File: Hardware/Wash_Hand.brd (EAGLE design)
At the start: 71.1 x 48.3 mm, 87 parts, among them IC1 LM358D, IC2 LP298XS, IC3 405016TSSOP, J1 I2C, J2 ICSP, J3 SPI, J4 9V_CONN, J5 EXT_VCC, J6 6_PIN_SERIAL_CABLEPTH, Q1 16.0 Mhz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

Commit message: RELEASE-1.4-rc2
Signed-off-by: Konrad Rzeszutek Wilk <konrad@kernel.org>
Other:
- board text added: "v1.4-rc2"
- board text removed: "v1.4-rc1"
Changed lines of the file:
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@@
 <circle x="8.636" y="38.862" radius="0.254" width="0.254" layer="25"/>
 <circle x="8.636" y="38.862" radius="0.567959375" width="0.1524" layer="25"/>
-<text x="33.02" y="5.842" size="1.778" layer="26" ratio="14" rot="MR0">v1.4-rc1</text>
+<text x="33.02" y="5.842" size="1.778" layer="26" ratio="14" rot="MR0">v1.4-rc2</text>
 <text x="54.356" y="18.796" size="1.016" layer="25" ratio="14">#
 [  ]

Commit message: Board/Schematic: Add PNP to turn on/off the line sensor
.. which we don't have to have on all the time.

Signed-off-by: Konrad Rzeszutek Wilk <konrad@kernel.org>
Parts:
- added T1: PNP, zetex:SOT-23
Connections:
- new net ON_OFF_PNP: T1.3, U2.22
- net VCC: now also T1.2
- net V_POS: now also T1.1
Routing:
- net ON_OFF_PNP: track 0.00 -> 59.3 mm, vias 0 -> 4
- net V_POS: track 33.5 -> 37.3 mm
- net VCC: track 247.9 -> 249.3 mm
- net D0: track 108.8 -> 107.6 mm
- net TX: track 59.1 -> 58.0 mm
- net D: track 12.8 -> 13.4 mm

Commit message: Board/Schematic: Remove 1K by RST/DTR
We haven't used it for two releases and it does
not help with DTR at all.

Signed-off-by: Konrad Rzeszutek Wilk <konrad@kernel.org>
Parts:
- removed R12: 1K, darnok_common:1206
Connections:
- net 0: no longer R12.1
- net RESET: no longer R12.2
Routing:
- net 0: track 390.9 -> 385.3 mm
- net RESET: track 59.3 -> 57.5 mm
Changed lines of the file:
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@@
 <attribute name="VALUE" x="35.56" y="19.304" size="0.6096" layer="27" font="vector" ratio="20" rot="R180" align="bottom-center"/>
-</element>
-<element name="R12" library="darnok_common" package="1206" value="1K" x="23.876" y="10.414" smashed="yes" rot="R90">
-<attribute name="NAME" x="25.527" y="11.43" size="0.6096" layer="25" font="vector" ratio="20" rot="R90" align="bottom-center"/>
-<attribute name="VALUE" x="25.273" y="8.636" size="0.6096" layer="27" font="vector" ratio="20" rot="R90" align="top-center"/>
 </element>
 <element name="R13" library="darnok_common" package="1206" value="1M" x="46.736" y="15.494" smashed="yes" rot="R270">
@@
 <contactref element="U2" pad="29"/>
 <contactref element="J2" pad="5"/>
-<contactref element="R12" pad="2"/>
 <wire x1="60.706" y1="2.286" x2="60.706" y2="8.636" width="0.3048" layer="16"/>
 <wire x1="55.626" y1="2.54" x2="57.404" y2="0.762" width="0.3048" layer="16" curve="90"/>
@@
 <wire x1="25.784" y1="11.814" x2="25.654" y2="11.684" width="0.3048" layer="1" curve="90"/>
 <via x="25.654" y="11.684" extent="1-16" drill="0.35"/>
-<wire x1="25.654" y1="11.684" x2="24.006" y2="11.684" width="0.3048" layer="1"/>
-<wire x1="24.006" y1="11.684" x2="23.876" y2="11.814" width="0.3048" layer="1" curve="-90"/>
 <wire x1="25.654" y1="11.684" x2="25.784" y2="11.814" width="0.3048" layer="1" curve="-90"/>
 <wire x1="25.784" y1="11.814" x2="27.432" y2="11.814" width="0.3048" layer="1"/>
@@
 <contactref element="C2" pad="2"/>
 <contactref element="C1" pad="2"/>
-<contactref element="R12" pad="1"/>
 <contactref element="Y1" pad="2"/>
 <wire x1="27.432" y1="15.618" x2="29.24405" y2="13.29795" width="0.3048" layer="1"/>
@@
 <wire x1="7.366" y1="10.414" x2="7.366" y2="9.398" width="0.3048" layer="1"/>
 <wire x1="7.366" y1="9.398" x2="8.128" y2="8.636" width="0.3048" layer="1"/>
-<wire x1="23.876" y1="9.014" x2="18.288" y2="9.014" width="0.3048" layer="1"/>
 <wire x1="11.176" y1="9.014" x2="7.75" y2="9.014" width="0.3048" layer="1"/>
 <wire x1="7.75" y1="9.014" x2="7.366" y2="9.398" width="0.3048" layer="1" curve="-90"/>

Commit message: Board/Schematic: Rotate LED2 around..
We been soldering it the right way but the schematic
has it turned around.

Signed-off-by: Konrad Rzeszutek Wilk <konrad@kernel.org>
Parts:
- turned LED2 to 90 degrees
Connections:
- removed net INT_LED: LED2.C, R17.2
- new net N$15: LED2.A, R17.2
- net 0: now also LED2.C; no longer LED2.A
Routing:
- net N$15: track 0.00 -> 3.78 mm
- net INT_LED: track 3.78 -> 0.00 mm
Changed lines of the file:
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@@
 <attribute name="VALUE" x="62.865" y="16.256" size="0.6096" layer="27" font="vector" ratio="20" rot="R90" align="top-center"/>
 </element>
-<element name="LED2" library="adafruit" library_urn="urn:adsk.eagle:library:420" package="1206" package3d_urn="urn:adsk.eagle:package:6240349/1" value="" x="61.468" y="21.59" smashed="yes" rot="R270">
-<attribute name="NAME" x="62.738" y="22.86" size="0.6096" layer="25" rot="R270"/>
-<attribute name="VALUE" x="58.928" y="22.86" size="1.27" layer="27" rot="R270"/>
+<element name="LED2" library="adafruit" library_urn="urn:adsk.eagle:library:420" package="1206" package3d_urn="urn:adsk.eagle:package:6240349/1" value="" x="61.468" y="21.59" smashed="yes" rot="R90">
+<attribute name="NAME" x="60.198" y="20.32" size="0.6096" layer="25" rot="R90"/>
+<attribute name="VALUE" x="64.008" y="20.32" size="1.27" layer="27" rot="R90"/>
 </element>
 <element name="R18" library="darnok_common" package="1206" value="100K" x="25.908" y="31.496" smashed="yes" rot="R90">
@@
 <wire x1="20.32" y1="39.878" x2="19.304" y2="39.878" width="0.3048" layer="16"/>
 <wire x1="19.304" y1="39.878" x2="18.034" y2="39.878" width="0.3048" layer="16"/>
-<wire x1="47.622" y1="21.974" x2="60.43" y2="21.974" width="0.3048" layer="1"/>
+<wire x1="47.622" y1="21.974" x2="61.468" y2="21.974" width="0.3048" layer="1"/>
+<wire x1="61.468" y1="21.974" x2="61.846" y2="21.974" width="0.3048" layer="1"/>
 <wire x1="62.992" y1="13.462" x2="64.262" y2="12.192" width="0.3048" layer="1" curve="90"/>
 <wire x1="64.262" y1="12.192" x2="66.04" y2="10.414" width="0.3048" layer="1" curve="-90"/>
@@
 <via x="13.462" y="5.842" extent="1-16" drill="0.35"/>
 <contactref element="LED1" pad="A"/>
-<contactref element="LED2" pad="A"/>
-<wire x1="61.468" y1="23.012" x2="60.43" y2="21.974" width="0.3048" layer="1" curve="-90"/>
 <wire x1="62.992" y1="20.828" x2="61.846" y2="21.974" width="0.3048" layer="1" curve="90"/>
-<wire x1="61.846" y1="21.974" x2="60.43" y2="21.974" width="0.3048" layer="1"/>
 <contactref element="U1" pad="1"/>
 <contactref element="C12" pad="1"/>
@@
 <wire x1="64.262" y1="12.192" x2="62.862" y2="12.192" width="0.3048" layer="16"/>
 <wire x1="62.862" y1="12.192" x2="61.468" y2="13.586" width="0.3048" layer="16" curve="-90"/>
+<contactref element="LED2" pad="C"/>
+<wire x1="61.468" y1="23.012" x2="61.468" y2="21.974" width="0.3048" layer="1"/>
 </signal>
 <signal name="D0">
@@
 <wire x1="63.5" y1="33.274" x2="63.5" y2="34.544" width="0.3048" layer="16"/>
 <wire x1="58.674" y1="17.018" x2="59.306" y2="16.386" width="0.3048" layer="16" curve="90"/>
-<wire x1="59.306" y1="16.386" x2="61.468" y2="16.386" width="0.3048" layer="16"/>
+<wire x1="59.306" y1="16.386" x2="59.436" y2="16.386" width="0.3048" layer="16"/>
+<wire x1="59.436" y1="16.386" x2="61.468" y2="16.386" width="0.3048" layer="16"/>
 </signal>
 <signal name="N$11">
@@
 <wire x1="18.31" y1="17.932" x2="18.288" y2="18.418" width="0.3048" layer="1" curve="90"/>
 </signal>
-<signal name="INT_LED">
-<contactref element="LED2" pad="C"/>
-<contactref element="R17" pad="2"/>
-<wire x1="61.468" y1="20.168" x2="61.468" y2="16.386" width="0.3048" layer="1"/>
-</signal>
 <signal name="CD">
 <contactref element="U2" pad="19"/>
@@
 <wire x1="48.006" y1="37.338" x2="48.006" y2="36.576" width="0.3048" layer="1"/>
 </signal>
+<signal name="N$15">
+<contactref element="LED2" pad="A"/>
+<contactref element="R17" pad="2"/>
+<wire x1="61.468" y1="20.168" x2="61.468" y2="16.386" width="0.3048" layer="1"/>
+</signal>
 </signals>

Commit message: Board/Schematic: Add 6x2 connector for 7 segment display
so that we can extend it in the future if we want to
use other types and need a basic building block
(this board) to drive it easily.

Signed-off-by: Konrad Rzeszutek Wilk <konrad@kernel.org>
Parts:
- added J8: 2X6 FEMALE, SparkFun-Connectors:2X6
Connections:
- new net DP: U$5.PIN$3
- net 0: now also J8.8
- net A: now also J8.9
- net B: now also J8.1
- net C: now also J8.5
- net D: now also J8.11
- net D1: now also J8.2
- net D2: now also J8.4
- net D3: now also J8.6
- net D4: now also J8.12
- net E: now also J8.10
- net F: now also J8.7
- net G: now also J8.3
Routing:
- net D4: track 10.6 -> 51.1 mm
- net B: track 11.3 -> 30.5 mm
- net D3: track 88.8 -> 107.9 mm
- net G: track 10.0 -> 24.9 mm
- net D2: track 64.4 -> 78.5 mm
- net C: track 8.74 -> 21.7 mm
- net E: track 13.6 -> 26.5 mm
- net D: track 13.4 -> 22.2 mm
- net F: track 12.0 -> 20.5 mm
- net 0: track 384.8 -> 392.4 mm, vias 115 -> 116
- net A: track 12.7 -> 19.6 mm
- net PIN_C: track 80.4 -> 83.5 mm
- net D1: track 53.4 -> 56.2 mm
- net ON_OFF_PNP: track 59.3 -> 62.0 mm
- net PIN_D: track 29.2 -> 27.8 mm
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
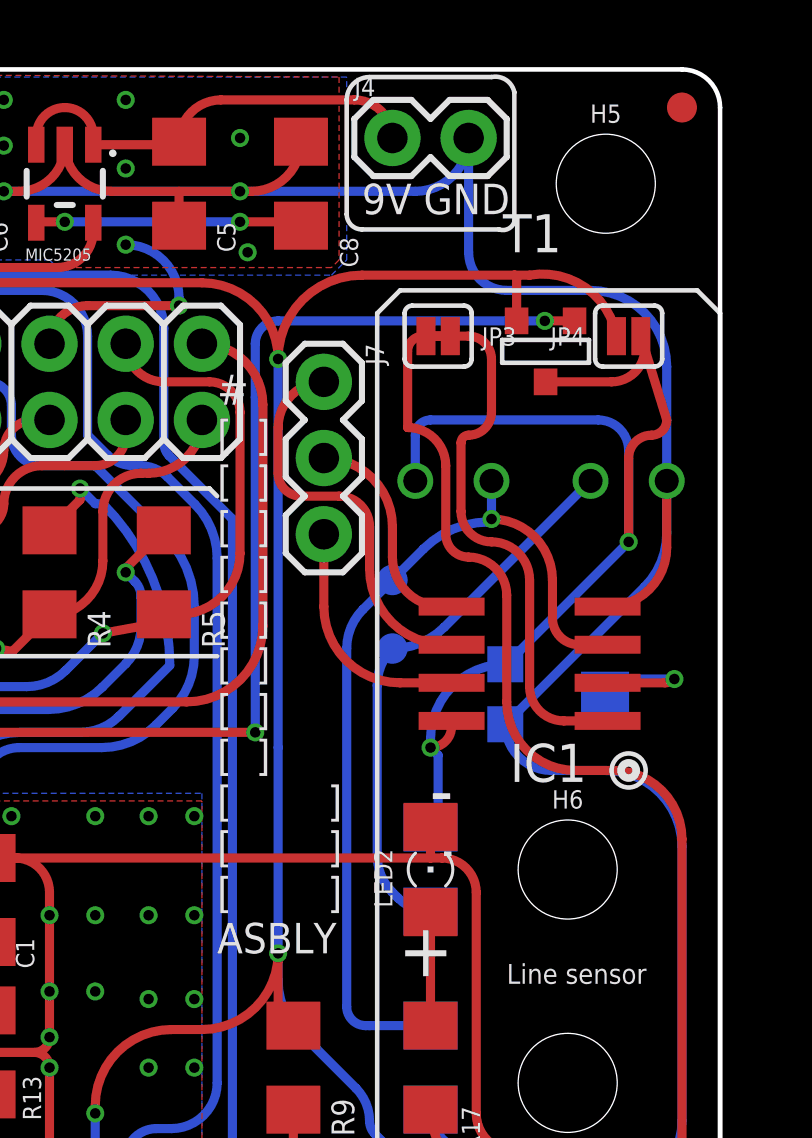
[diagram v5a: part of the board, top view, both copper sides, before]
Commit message: Board/Schematic: Add 1.2K resistor to transistor
Signed-off-by: Konrad Rzeszutek Wilk <konrad@kernel.org>
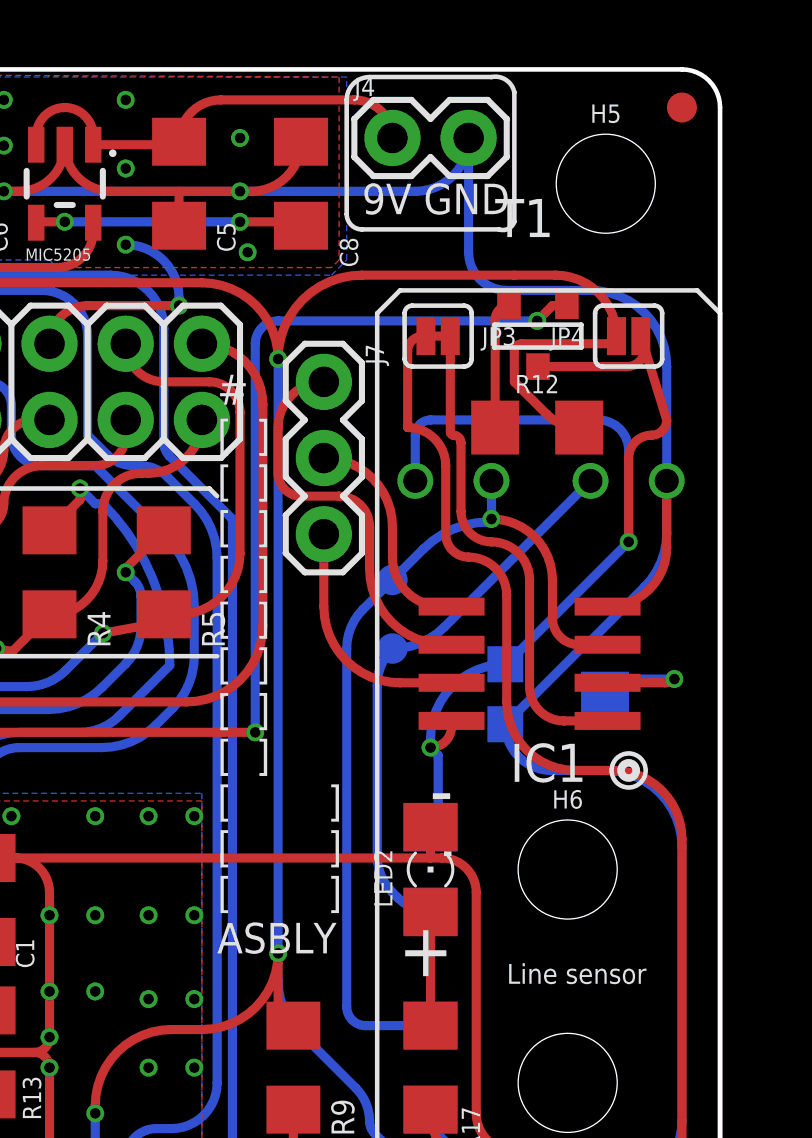
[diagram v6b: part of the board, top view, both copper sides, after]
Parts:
- added R12: 1.2K, darnok_common:1206
- moved T1 0.57 mm to (65.0, 39.4)
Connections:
- new net N$19: R12.1, T1.2
- net VCC: now also R12.2; no longer T1.2
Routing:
- net VCC: track 249.3 -> 255.3 mm
- net N$19: track 0.00 -> 4.25 mm
- net D0: track 107.6 -> 105.6 mm
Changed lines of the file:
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@@
 <attribute name="VALUE" x="55.88" y="39.116" size="0.6096" layer="27" font="vector" ratio="20" rot="R270"/>
 </element>
-<element name="T1" library="zetex" library_urn="urn:adsk.eagle:library:418" package="SOT-23" package3d_urn="urn:adsk.eagle:package:30981/1" value="PNP" x="65.278" y="38.862" smashed="yes">
-<attribute name="MF" value="" x="65.278" y="38.862" size="1.778" layer="27" display="off"/>
-<attribute name="MPN" value="DSS20200L-7" x="65.278" y="38.862" size="1.778" layer="27" display="off"/>
-<attribute name="NAME" x="63.881" y="42.164" size="1.27" layer="25" ratio="10"/>
-<attribute name="OC_FARNELL" value="unknown" x="65.278" y="38.862" size="1.778" layer="27" display="off"/>
-<attribute name="OC_NEWARK" value="25R4554" x="65.278" y="38.862" size="1.778" layer="27" display="off"/>
-<attribute name="POPULARITY" value="0" x="65.278" y="38.862" size="1.778" layer="27" display="off"/>
-<attribute name="VALUE" x="63.881" y="40.64" size="1.27" layer="27" ratio="10"/>
+<element name="T1" library="zetex" library_urn="urn:adsk.eagle:library:418" package="SOT-23" package3d_urn="urn:adsk.eagle:package:30981/1" value="PNP" x="65.024" y="39.37" smashed="yes">
+<attribute name="MF" value="" x="65.024" y="39.37" size="1.778" layer="27" display="off"/>
+<attribute name="MPN" value="DSS20200L-7" x="65.024" y="39.37" size="1.778" layer="27" display="off"/>
+<attribute name="NAME" x="63.627" y="42.672" size="1.27" layer="25" ratio="10"/>
+<attribute name="OC_FARNELL" value="unknown" x="65.024" y="39.37" size="1.778" layer="27" display="off"/>
+<attribute name="OC_NEWARK" value="25R4554" x="65.024" y="39.37" size="1.778" layer="27" display="off"/>
+<attribute name="POPULARITY" value="0" x="65.024" y="39.37" size="1.778" layer="27" display="off"/>
+<attribute name="VALUE" x="63.627" y="41.148" size="1.27" layer="27" ratio="10"/>
 </element>
 <element name="J8" library="SparkFun-Connectors" library_urn="urn:adsk.eagle:library:513" package="2X6" package3d_urn="urn:adsk.eagle:package:38277/1" value="2X6 FEMALE" x="41.148" y="36.576" smashed="yes">
@@
 <attribute name="PROD_ID" value="CONN-12423" x="41.148" y="36.576" size="1.778" layer="27" display="off"/>
 <attribute name="VALUE" x="39.878" y="34.163" size="0.6096" layer="27" font="vector" ratio="20"/>
+</element>
+<element name="R12" library="darnok_common" package="1206" value="1.2K" x="65.024" y="36.322" smashed="yes">
+<attribute name="NAME" x="65.024" y="37.465" size="0.6096" layer="25" font="vector" ratio="20" align="bottom-center"/>
+<attribute name="VALUE" x="65.024" y="35.179" size="0.6096" layer="27" font="vector" ratio="20" align="top-center"/>
 </element>
 </elements>
@@
 <contactref element="JP2" pad="2"/>
 <contactref element="TP1" pad="P$1"/>
-<contactref element="JP4" pad="1"/>
 <contactref element="IC2" pad="1"/>
 <contactref element="IC2" pad="3"/>
@@
 <wire x1="59.436" y1="13.208" x2="59.61560625" y2="12.77439375" width="0.3048" layer="16" curve="45"/>
 <wire x1="59.61560625" y1="12.77439375" x2="63.5" y2="8.89" width="0.3048" layer="16"/>
-<wire x1="56.388" y1="38.608" x2="56.388" y2="25.654" width="0.3048" layer="16"/>
-<wire x1="56.388" y1="25.654" x2="56.388" y2="18.796" width="0.3048" layer="16"/>
+<wire x1="56.388" y1="38.608" x2="56.388" y2="18.796" width="0.3048" layer="16"/>
 <wire x1="56.388" y1="18.796" x2="56.388" y2="17.88395" width="0.3048" layer="16"/>
 <wire x1="56.388" y1="17.88395" x2="57.088" y2="16.194" width="0.3048" layer="16" curve="45"/>
@@
 <wire x1="52.832" y1="16.256" x2="53.848" y2="16.256" width="0.3048" layer="1"/>
 <wire x1="56.388" y1="38.608" x2="59.182" y2="41.402" width="0.3048" layer="1" curve="-90"/>
-<wire x1="64.77" y1="41.402" x2="67.6656" y2="39.37" width="0.3048" layer="1" curve="-90"/>
 <wire x1="59.182" y1="41.402" x2="64.262" y2="41.402" width="0.3048" layer="1"/>
-<wire x1="64.262" y1="41.402" x2="64.77" y2="41.402" width="0.3048" layer="1"/>
 <wire x1="56.388" y1="18.796" x2="56.388" y2="16.894" width="0.3048" layer="1"/>
 <wire x1="56.388" y1="16.894" x2="56.896" y2="16.386" width="0.3048" layer="1" curve="90"/>
@@
 <wire x1="21.59" y1="33.782" x2="22.098" y2="34.29" width="0.3048" layer="1" curve="-90"/>
 <wire x1="22.098" y1="34.29" x2="22.99" y2="34.29" width="0.3048" layer="1"/>
-<contactref element="T1" pad="2"/>
-<wire x1="64.3382" y1="39.878" x2="64.3382" y2="41.3258" width="0.3048" layer="1"/>
-<wire x1="64.3382" y1="41.3258" x2="64.262" y2="41.402" width="0.3048" layer="1" curve="90"/>
+<contactref element="JP4" pad="1"/>
+<wire x1="64.262" y1="41.402" x2="65.6336" y2="41.402" width="0.3048" layer="1"/>
+<wire x1="65.6336" y1="41.402" x2="67.6656" y2="39.37" width="0.3048" layer="1" curve="-90"/>
+<contactref element="R12" pad="2"/>
+<wire x1="65.334865625" y1="36.773134375" x2="66.424" y2="36.322" width="0.3048" layer="1" curve="45"/>
+<wire x1="67.6656" y1="39.37" x2="67.4116" y2="39.116" width="0.3048" layer="1" curve="-90"/>
+<wire x1="64.516" y1="39.116" x2="64.262" y2="38.862" width="0.3048" layer="1" curve="90"/>
+<wire x1="64.262" y1="38.862" x2="64.262" y2="37.846" width="0.3048" layer="1"/>
+<wire x1="64.262" y1="37.846" x2="65.334865625" y2="36.773134375" width="0.3048" layer="1"/>
+<wire x1="67.4116" y1="39.116" x2="64.516" y2="39.116" width="0.3048" layer="1"/>
 </signal>
 <signal name="0">
@@
 <via x="36.83" y="12.446" extent="1-16" drill="0.35"/>
 <wire x1="32.258" y1="10.922" x2="31.34465625" y2="10.922" width="0.3048" layer="1"/>
-<wire x1="62.738" y1="39.37" x2="63.5" y2="38.608" width="0.3048" layer="1" curve="-90"/>
-<wire x1="63.5" y1="36.83" x2="62.738" y2="36.068" width="0.3048" layer="1" curve="-90"/>
-<wire x1="62.738" y1="36.068" x2="62.484" y2="35.814" width="0.3048" layer="1" curve="90"/>
 <wire x1="64.77" y1="27.686" x2="65.913" y2="26.543" width="0.3048" layer="1" curve="90"/>
 <wire x1="65.913" y1="26.543" x2="67.31" y2="26.543" width="0.3048" layer="1"/>
-<wire x1="63.5" y1="38.608" x2="63.5" y2="36.83" width="0.3048" layer="1"/>
 <wire x1="68.58" y1="8.89" x2="68.58" y2="10.668" width="0.3048" layer="1"/>
 <wire x1="68.58" y1="10.668" x2="69.342" y2="11.43" width="0.3048" layer="1" curve="-90"/>
@@
 <wire x1="69.85" y1="11.938" x2="69.85" y2="22.606" width="0.3048" layer="1"/>
 <wire x1="69.85" y1="22.606" x2="67.564" y2="24.892" width="0.3048" layer="1" curve="90"/>
-<wire x1="61.3156" y1="39.37" x2="62.738" y2="39.37" width="0.3048" layer="1"/>
 <wire x1="62.1284" y1="39.37" x2="61.3156" y2="39.37" width="0.3048" layer="1"/>
 <contactref element="R17" pad="1"/>
@@
 <wire x1="60.706" y1="38.862" x2="61.214" y2="39.37" width="0.3048" layer="1" curve="-90"/>
 <wire x1="61.976" y1="32.766" x2="61.976" y2="35.052" width="0.3048" layer="1"/>
-<wire x1="62.484" y1="35.814" x2="62.484" y2="33.528" width="0.3048" layer="1"/>
 <wire x1="62.484" y1="33.528" x2="63.5" y2="32.512" width="0.3048" layer="1" curve="90"/>
 <wire x1="63.5" y1="32.512" x2="64.77" y2="31.242" width="0.3048" layer="1" curve="-90"/>
@@
 <wire x1="33.60239375" y1="12.26639375" x2="32.258" y2="10.922" width="0.3048" layer="1"/>
 <wire x1="36.576" y1="12.7" x2="35.814" y2="12.7" width="0.3048" layer="1"/>
+<wire x1="62.1284" y1="39.37" x2="62.1284" y2="36.1696" width="0.3048" layer="1"/>
+<wire x1="62.1284" y1="36.1696" x2="62.23" y2="36.068" width="0.3048" layer="1" curve="90"/>
+<wire x1="62.23" y1="36.068" x2="62.484" y2="35.814" width="0.3048" layer="1" curve="-90"/>
+<wire x1="62.484" y1="35.814" x2="62.484" y2="33.528" width="0.3048" layer="1"/>
 </signal>
 <signal name="SDA">
@@
 <wire x1="60.96" y1="36.068" x2="60.96" y2="34.544" width="0.3048" layer="16"/>
 <contactref element="T1" pad="1"/>
-<wire x1="65.3034" y1="37.846" x2="67.5051375" y2="37.846" width="0.3048" layer="1"/>
-<wire x1="67.5051375" y1="37.846" x2="68.608434375" y2="38.949296875" width="0.3048" layer="1" curve="90"/>
+<wire x1="65.0494" y1="38.354" x2="68.0131375" y2="38.354" width="0.3048" layer="1"/>
+<wire x1="68.0131375" y1="38.354" x2="68.608434375" y2="38.949296875" width="0.3048" layer="1" curve="90"/>
 </signal>
 <signal name="NEG_IN">
@@
 <contactref element="U2" pad="22"/>
 <contactref element="T1" pad="3"/>
-<wire x1="66.2686" y1="39.878" x2="65.278" y2="39.878" width="0.3048" layer="1"/>
-<via x="65.278" y="39.878" extent="1-16" drill="0.35"/>
+<wire x1="66.0146" y1="40.386" x2="65.532" y2="40.386" width="0.3048" layer="1"/>
+<wire x1="65.532" y1="40.386" x2="65.024" y2="39.878" width="0.3048" layer="1"/>
+<via x="65.024" y="39.878" extent="1-16" drill="0.35"/>
 <wire x1="31.2674" y1="11.754" x2="31.566" y2="11.754" width="0.3048" layer="1"/>
 <wire x1="34.036" y1="14.986" x2="34.036" y2="13.716" width="0.3048" layer="1"/>
@@
 <wire x1="39.878" y1="24.427578125" x2="40.386" y2="25.654" width="0.3048" layer="16" curve="-45"/>
 <wire x1="39.878" y1="23.473209375" x2="39.878" y2="24.427578125" width="0.3048" layer="16"/>
-<wire x1="65.278" y1="39.878" x2="56.388" y2="39.878" width="0.3048" layer="16"/>
+<wire x1="65.024" y1="39.878" x2="56.388" y2="39.878" width="0.3048" layer="16"/>
 <wire x1="56.388" y1="39.878" x2="55.626" y2="39.116" width="0.3048" layer="16" curve="90"/>
-<wire x1="55.626" y1="39.116" x2="55.626" y2="37.338" width="0.3048" layer="16"/>
-<wire x1="55.626" y1="37.338" x2="55.626" y2="26.162" width="0.3048" layer="16"/>
+<wire x1="55.626" y1="39.116" x2="55.626" y2="26.162" width="0.3048" layer="16"/>
 <via x="55.626" y="26.162" extent="1-16" drill="0.35"/>
 <wire x1="55.626" y1="26.162" x2="41.612421875" y2="26.162" width="0.3048" layer="1"/>
@@
 <contactref element="U$5" pad="PIN$3"/>
 </signal>
+<signal name="N$19">
+<contactref element="T1" pad="2"/>
+<contactref element="R12" pad="1"/>
+<wire x1="63.624" y1="36.322" x2="63.624" y2="39.9258" width="0.3048" layer="1"/>
+<wire x1="63.624" y1="39.9258" x2="64.0842" y2="40.386" width="0.3048" layer="1" curve="-90"/>
+</signal>
 </signals>
